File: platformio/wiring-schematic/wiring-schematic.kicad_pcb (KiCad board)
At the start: 2 copper layers, 5 parts, among them U0 LSM9DS1, U1 LSM9DS1, U2 LSM9DS1, U3 LSM9DS1

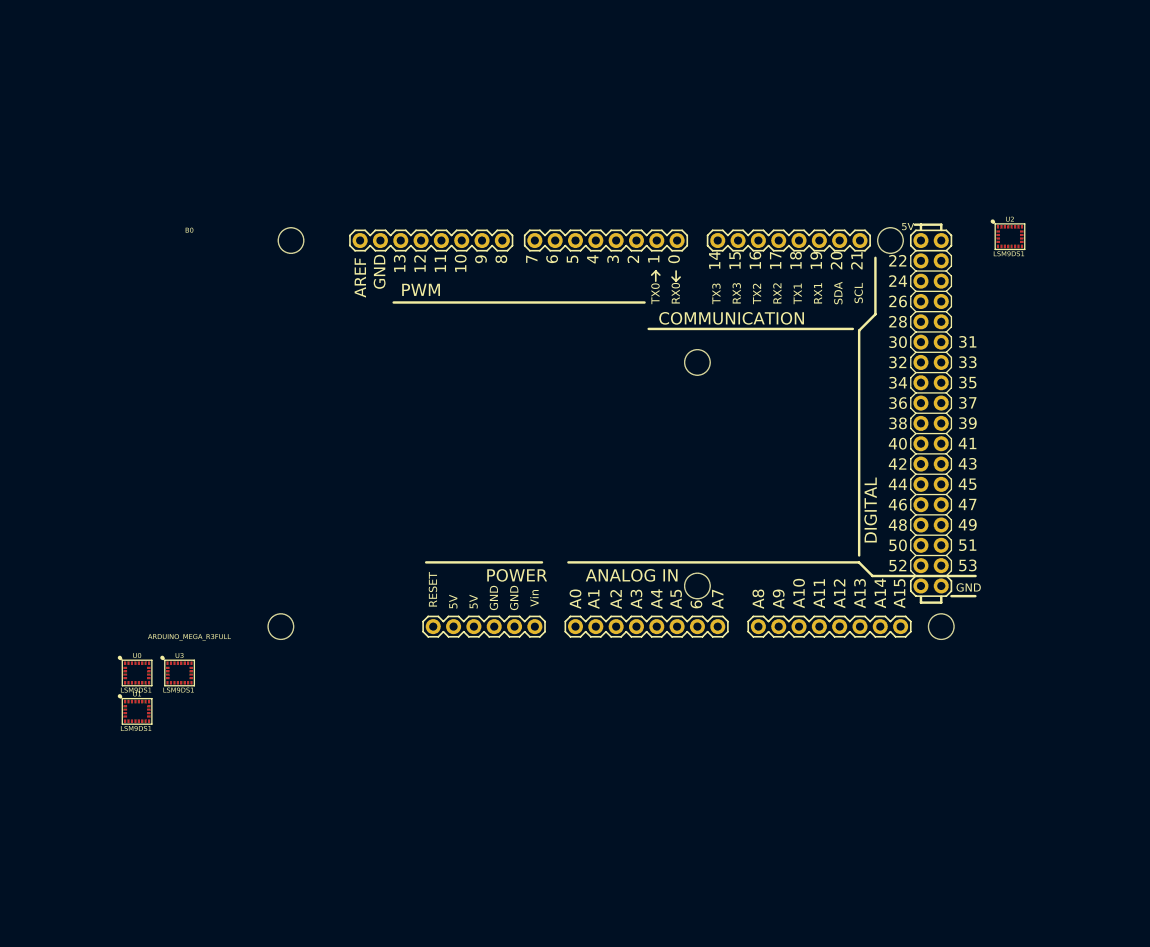
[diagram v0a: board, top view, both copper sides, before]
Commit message: reorganised kicad schematic
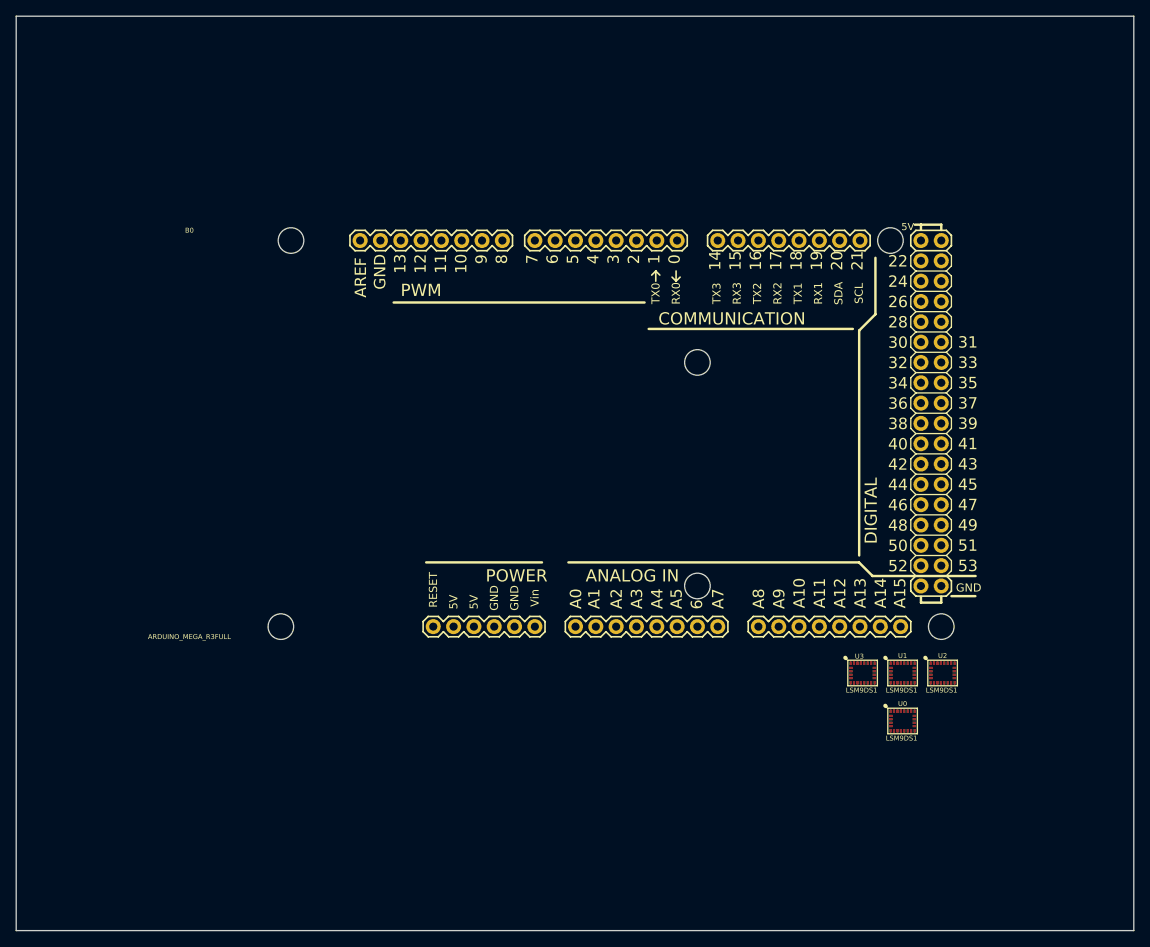
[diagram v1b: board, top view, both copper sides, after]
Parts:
- moved U0 95.9 mm to (695.0, -331.0)
- moved U1 95.8 mm to (695.0, -337.0)
- moved U3 85.4 mm to (690.0, -337.0)
- moved U2 55.2 mm to (700.0, -337.0)
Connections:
- net /CS_MAG_IMU0 renamed /CS_M_0
- net /CS_MAG_IMU1 renamed /CS_M_1
- net /CS_MAG_IMU2 renamed /CS_M_2
- net /CS_MAG_IMU3 renamed /CS_M_3
- B0 pad 0: /CS Accel IMU 0 -> (no net)
- B0 pad 1: /CS Accel IMU 1 -> (no net)
- B0 pad 10: unconnected-(B0-Pad10) -> (no net)
- B0 pad 11: unconnected-(B0-Pad11) -> (no net)
- B0 pad 12: unconnected-(B0-Pad12) -> (no net)
- B0 pad 13: unconnected-(B0-Pad13) -> (no net)
- B0 pad 14: unconnected-(B0-Pad14) -> (no net)
- B0 pad 15: unconnected-(B0-Pad15) -> (no net)
- B0 pad 16: unconnected-(B0-Pad16) -> (no net)
- B0 pad 17: unconnected-(B0-Pad17) -> (no net)
- B0 pad 18: unconnected-(B0-Pad18) -> (no net)
- B0 pad 19: unconnected-(B0-Pad19) -> (no net)
- B0 pad 2: /CS Accel IMU 2 -> (no net)
- B0 pad 24: unconnected-(B0-Pad24) -> (no net)
- B0 pad 25: unconnected-(B0-Pad25) -> (no net)
- B0 pad 26: unconnected-(B0-Pad26) -> (no net)
- B0 pad 27: unconnected-(B0-Pad27) -> (no net)
- B0 pad 28: unconnected-(B0-Pad28) -> (no net)
- B0 pad 29: unconnected-(B0-Pad29) -> (no net)
- B0 pad 3: /CS Accel IMU 3 -> (no net)
- B0 pad 3.3V: unconnected-(B0-Pad3.3V) -> (no net)
- B0 pad 30: unconnected-(B0-Pad30) -> (no net)
- B0 pad 31: unconnected-(B0-Pad31) -> (no net)
- B0 pad 32: unconnected-(B0-Pad32) -> (no net)
- B0 pad 33: unconnected-(B0-Pad33) -> (no net)
- B0 pad 34: unconnected-(B0-Pad34) -> (no net)
- B0 pad 35: unconnected-(B0-Pad35) -> (no net)
- B0 pad 36: unconnected-(B0-Pad36) -> (no net)
- B0 pad 37: unconnected-(B0-Pad37) -> (no net)
- B0 pad 38: unconnected-(B0-Pad38) -> (no net)
- B0 pad 39: unconnected-(B0-Pad39) -> (no net)
- B0 pad 4: unconnected-(B0-Pad4) -> (no net)
- B0 pad 40: unconnected-(B0-Pad40) -> (no net)
- B0 pad 41: unconnected-(B0-Pad41) -> (no net)
- B0 pad 42: unconnected-(B0-Pad42) -> (no net)
- B0 pad 43: unconnected-(B0-Pad43) -> (no net)
- B0 pad 44: unconnected-(B0-Pad44) -> (no net)
- B0 pad 45: unconnected-(B0-Pad45) -> (no net)
- B0 pad 46: unconnected-(B0-Pad46) -> (no net)
- B0 pad 47: unconnected-(B0-Pad47) -> (no net)
- B0 pad 48: unconnected-(B0-Pad48) -> (no net)
- B0 pad 49: unconnected-(B0-Pad49) -> (no net)
- B0 pad 5: unconnected-(B0-Pad5) -> (no net)
- B0 pad 50: /SPI MISO -> (no net)
- B0 pad 53: unconnected-(B0-Pad53) -> (no net)
- B0 pad 5V@0: unconnected-(B0-Pad5V@0) -> (no net)
- B0 pad 5V@1: unconnected-(B0-Pad5V@1) -> (no net)
- B0 pad 5V@2: unconnected-(B0-Pad5V@2) -> (no net)
- B0 pad 6: unconnected-(B0-Pad6) -> (no net)
- B0 pad 7: unconnected-(B0-Pad7) -> (no net)
- B0 pad 8: unconnected-(B0-Pad8) -> (no net)
- B0 pad 9: unconnected-(B0-Pad9) -> (no net)
- B0 pad A0: unconnected-(B0-PadA0) -> (no net)
- B0 pad A1: unconnected-(B0-PadA1) -> (no net)
- B0 pad A10: unconnected-(B0-PadA10) -> (no net)
- B0 pad A11: unconnected-(B0-PadA11) -> (no net)
- B0 pad A12: unconnected-(B0-PadA12) -> (no net)
- B0 pad A13: unconnected-(B0-PadA13) -> (no net)
- B0 pad A14: unconnected-(B0-PadA14) -> (no net)
- B0 pad A15: unconnected-(B0-PadA15) -> (no net)
- B0 pad A2: unconnected-(B0-PadA2) -> (no net)
- B0 pad A3: unconnected-(B0-PadA3) -> (no net)
- B0 pad A4: unconnected-(B0-PadA4) -> (no net)
- B0 pad A5: unconnected-(B0-PadA5) -> (no net)
- B0 pad A6: unconnected-(B0-PadA6) -> (no net)
- B0 pad A7: unconnected-(B0-PadA7) -> (no net)
- B0 pad A8: unconnected-(B0-PadA8) -> (no net)
- B0 pad A9: unconnected-(B0-PadA9) -> (no net)
- B0 pad AREF: unconnected-(B0-PadAREF) -> (no net)
- B0 pad RESE: unconnected-(B0-PadRESE) -> (no net)
- U0 pad 10: unconnected-(U0-Pad10) -> (no net)
- U0 pad 11: unconnected-(U0-Pad11) -> (no net)
- U0 pad 12: unconnected-(U0-Pad12) -> (no net)
- U0 pad 13: unconnected-(U0-Pad13) -> (no net)
- U0 pad 21: unconnected-(U0-Pad21) -> (no net)
- U0 pad 24: unconnected-(U0-Pad24) -> (no net)
- U0 pad 5: unconnected-(U0-Pad5) -> (no net)
- U0 pad 6: unconnected-(U0-Pad6) -> (no net)
- U0 pad 7: /CS Accel IMU 0 -> (no net)
- U0 pad 9: unconnected-(U0-Pad9) -> (no net)
- U1 pad 10: unconnected-(U1-Pad10) -> (no net)
- U1 pad 11: unconnected-(U1-Pad11) -> (no net)
- U1 pad 12: unconnected-(U1-Pad12) -> (no net)
- U1 pad 13: unconnected-(U1-Pad13) -> (no net)
- U1 pad 21: unconnected-(U1-Pad21) -> (no net)
- U1 pad 24: unconnected-(U1-Pad24) -> (no net)
- U1 pad 5: unconnected-(U1-Pad5) -> (no net)
- U1 pad 6: unconnected-(U1-Pad6) -> (no net)
- U1 pad 7: /CS Accel IMU 1 -> (no net)
- U1 pad 9: unconnected-(U1-Pad9) -> (no net)
- U2 pad 10: unconnected-(U2-Pad10) -> (no net)
- U2 pad 11: unconnected-(U2-Pad11) -> (no net)
- U2 pad 12: unconnected-(U2-Pad12) -> (no net)
- U2 pad 13: unconnected-(U2-Pad13) -> (no net)
- U2 pad 21: unconnected-(U2-Pad21) -> (no net)
- U2 pad 24: unconnected-(U2-Pad24) -> (no net)
- U2 pad 5: unconnected-(U2-Pad5) -> (no net)
- U2 pad 6: unconnected-(U2-Pad6) -> (no net)
- U2 pad 7: /CS Accel IMU 2 -> (no net)
- U2 pad 9: unconnected-(U2-Pad9) -> (no net)
- U3 pad 10: unconnected-(U3-Pad10) -> (no net)
- U3 pad 11: unconnected-(U3-Pad11) -> (no net)
- U3 pad 12: unconnected-(U3-Pad12) -> (no net)
- U3 pad 13: unconnected-(U3-Pad13) -> (no net)
- U3 pad 21: unconnected-(U3-Pad21) -> (no net)
- U3 pad 24: unconnected-(U3-Pad24) -> (no net)
- U3 pad 5: unconnected-(U3-Pad5) -> (no net)
- U3 pad 6: unconnected-(U3-Pad6) -> (no net)
- U3 pad 7: /CS Accel IMU 3 -> (no net)
- U3 pad 9: unconnected-(U3-Pad9) -> (no net)
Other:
- board outline added: 139.7 x 114.3 mm

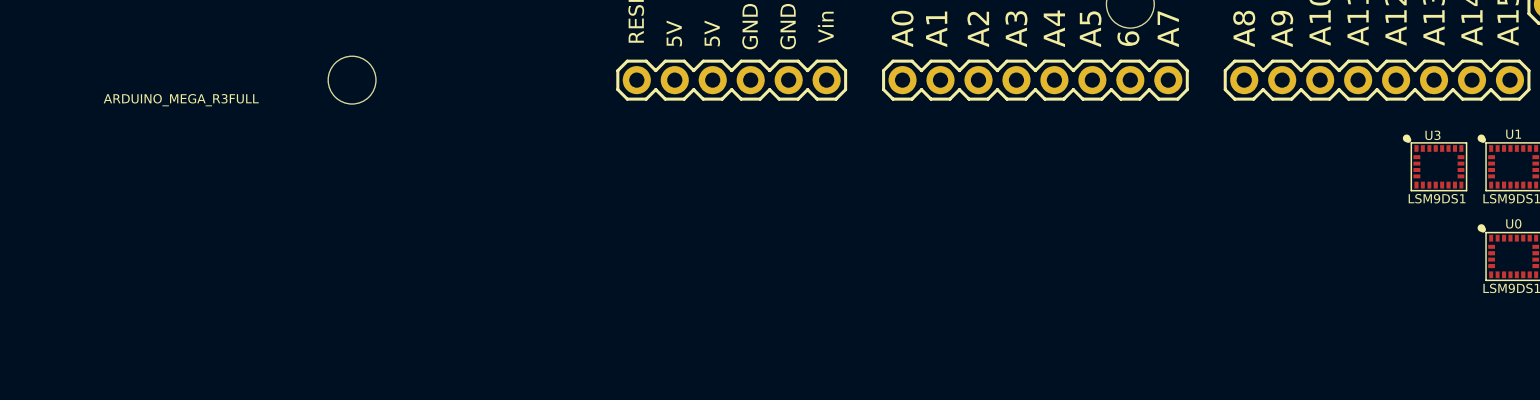
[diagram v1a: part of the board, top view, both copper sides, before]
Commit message: Finalised kicad schematic, and exported SVG
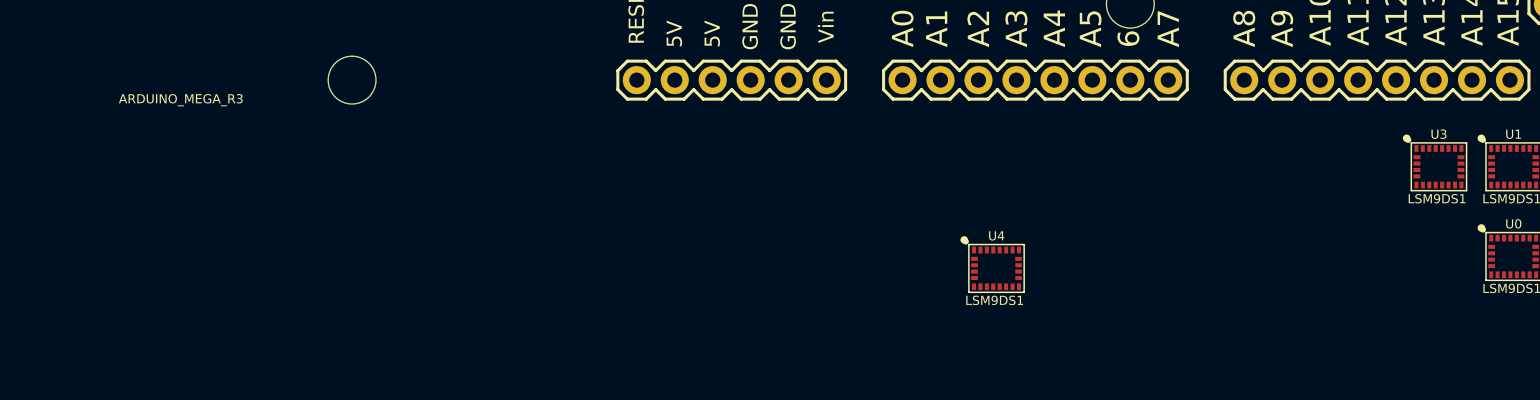
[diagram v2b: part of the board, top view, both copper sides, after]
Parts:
- added U4: LSM9DS1, SparkFun-Silicon-Custom:LGA-24-3.5X3, F.Cu at (660.4, -330.2)
- B0: value ARDUINO_MEGA_R3FULL -> ARDUINO_MEGA_R3
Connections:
- net +5V renamed 5V
- B0 pad 0: (no net) -> unconnected-(B0-Pad0)
- B0 pad 1: (no net) -> unconnected-(B0-Pad1)
- B0 pad 10: (no net) -> unconnected-(B0-Pad10)
- B0 pad 11: (no net) -> unconnected-(B0-Pad11)
- B0 pad 12: (no net) -> unconnected-(B0-Pad12)
- B0 pad 13: (no net) -> unconnected-(B0-Pad13)
- B0 pad 14: (no net) -> unconnected-(B0-Pad14)
- B0 pad 15: (no net) -> unconnected-(B0-Pad15)
- B0 pad 16: (no net) -> unconnected-(B0-Pad16)
- B0 pad 17: (no net) -> unconnected-(B0-Pad17)
- B0 pad 18: (no net) -> unconnected-(B0-Pad18)
- B0 pad 19: (no net) -> unconnected-(B0-Pad19)
- B0 pad 2: (no net) -> unconnected-(B0-Pad2)
- B0 pad 20: /CS_M_0 -> unconnected-(B0-Pad20)
- B0 pad 21: /CS_M_1 -> unconnected-(B0-Pad21)
- B0 pad 22: /CS_M_2 -> unconnected-(B0-Pad22)
- B0 pad 23: /CS_M_3 -> unconnected-(B0-Pad23)
- B0 pad 24: (no net) -> unconnected-(B0-Pad24)
- B0 pad 25: (no net) -> unconnected-(B0-Pad25)
- B0 pad 26: (no net) -> unconnected-(B0-Pad26)
- B0 pad 27: (no net) -> /CS_MAG_0
- B0 pad 28: (no net) -> /CS_ACC_0
- B0 pad 29: (no net) -> /CS_MAG_1
- B0 pad 3: (no net) -> unconnected-(B0-Pad3)
- B0 pad 3.3V: (no net) -> unconnected-(B0-Pad3.3V)
- B0 pad 30: (no net) -> /CS_ACC_1
- B0 pad 31: (no net) -> /CS_MAG_2
- B0 pad 32: (no net) -> /CS_ACC_2
- B0 pad 33: (no net) -> /CS_MAG_3
- B0 pad 34: (no net) -> /CS_ACC_3
- B0 pad 35: (no net) -> /CS_MAG_4
- B0 pad 36: (no net) -> /CS_ACC_4
- B0 pad 37: (no net) -> unconnected-(B0-Pad37)
- B0 pad 38: (no net) -> unconnected-(B0-Pad38)
- B0 pad 39: (no net) -> unconnected-(B0-Pad39)
- B0 pad 4: (no net) -> unconnected-(B0-Pad4)
- B0 pad 40: (no net) -> unconnected-(B0-Pad40)
- B0 pad 41: (no net) -> unconnected-(B0-Pad41)
- B0 pad 42: (no net) -> unconnected-(B0-Pad42)
- B0 pad 43: (no net) -> unconnected-(B0-Pad43)
- B0 pad 44: (no net) -> unconnected-(B0-Pad44)
- B0 pad 45: (no net) -> unconnected-(B0-Pad45)
- B0 pad 46: (no net) -> unconnected-(B0-Pad46)
- B0 pad 47: (no net) -> unconnected-(B0-Pad47)
- B0 pad 48: (no net) -> unconnected-(B0-Pad48)
- B0 pad 49: (no net) -> unconnected-(B0-Pad49)
- B0 pad 5: (no net) -> unconnected-(B0-Pad5)
- B0 pad 50: (no net) -> unconnected-(B0-Pad50)
- B0 pad 53: (no net) -> unconnected-(B0-Pad53)
- B0 pad 5V@0: (no net) -> unconnected-(B0-Pad5V@0)
- B0 pad 5V@1: (no net) -> unconnected-(B0-Pad5V@1)
- B0 pad 5V@2: (no net) -> unconnected-(B0-Pad5V@2)
- B0 pad 6: (no net) -> unconnected-(B0-Pad6)
- B0 pad 7: (no net) -> unconnected-(B0-Pad7)
- B0 pad 8: (no net) -> unconnected-(B0-Pad8)
- B0 pad 9: (no net) -> unconnected-(B0-Pad9)
- B0 pad A0: (no net) -> unconnected-(B0-PadA0)
- B0 pad A1: (no net) -> unconnected-(B0-PadA1)
- B0 pad A10: (no net) -> unconnected-(B0-PadA10)
- B0 pad A11: (no net) -> unconnected-(B0-PadA11)
- B0 pad A12: (no net) -> unconnected-(B0-PadA12)
- B0 pad A13: (no net) -> unconnected-(B0-PadA13)
- B0 pad A14: (no net) -> unconnected-(B0-PadA14)
- B0 pad A15: (no net) -> unconnected-(B0-PadA15)
- B0 pad A2: (no net) -> unconnected-(B0-PadA2)
- B0 pad A3: (no net) -> unconnected-(B0-PadA3)
- B0 pad A4: (no net) -> unconnected-(B0-PadA4)
- B0 pad A5: (no net) -> unconnected-(B0-PadA5)
- B0 pad A6: (no net) -> unconnected-(B0-PadA6)
- B0 pad A7: (no net) -> unconnected-(B0-PadA7)
- B0 pad A8: (no net) -> unconnected-(B0-PadA8)
- B0 pad A9: (no net) -> unconnected-(B0-PadA9)
- B0 pad AREF: (no net) -> unconnected-(B0-PadAREF)
- B0 pad RESE: (no net) -> unconnected-(B0-PadRESE)
- U0 pad 10: (no net) -> unconnected-(U0-Pad10)
- U0 pad 11: (no net) -> unconnected-(U0-Pad11)
- U0 pad 12: (no net) -> unconnected-(U0-Pad12)
- U0 pad 13: (no net) -> unconnected-(U0-Pad13)
- U0 pad 21: (no net) -> unconnected-(U0-Pad21)
- U0 pad 24: (no net) -> unconnected-(U0-Pad24)
- U0 pad 5: (no net) -> unconnected-(U0-Pad5)
- U0 pad 6: (no net) -> unconnected-(U0-Pad6)
- U0 pad 7: (no net) -> /CS_ACC_0
- U0 pad 8: /CS_M_0 -> /CS_MAG_0
- U0 pad 9: (no net) -> unconnected-(U0-Pad9)
- U1 pad 10: (no net) -> unconnected-(U1-Pad10)
- U1 pad 11: (no net) -> unconnected-(U1-Pad11)
- U1 pad 12: (no net) -> unconnected-(U1-Pad12)
- U1 pad 13: (no net) -> unconnected-(U1-Pad13)
- U1 pad 21: (no net) -> unconnected-(U1-Pad21)
- U1 pad 24: (no net) -> unconnected-(U1-Pad24)
- U1 pad 5: (no net) -> unconnected-(U1-Pad5)
- U1 pad 6: (no net) -> unconnected-(U1-Pad6)
- U1 pad 7: (no net) -> /CS_ACC_1
- U1 pad 8: /CS_M_1 -> /CS_MAG_1
- U1 pad 9: (no net) -> unconnected-(U1-Pad9)
- U2 pad 10: (no net) -> unconnected-(U2-Pad10)
- U2 pad 11: (no net) -> unconnected-(U2-Pad11)
- U2 pad 12: (no net) -> unconnected-(U2-Pad12)
- U2 pad 13: (no net) -> unconnected-(U2-Pad13)
- U2 pad 21: (no net) -> unconnected-(U2-Pad21)
- U2 pad 24: (no net) -> unconnected-(U2-Pad24)
- U2 pad 5: (no net) -> unconnected-(U2-Pad5)
- U2 pad 6: (no net) -> unconnected-(U2-Pad6)
- U2 pad 7: (no net) -> /CS_ACC_2
- U2 pad 8: /CS_M_2 -> /CS_MAG_2
- U2 pad 9: (no net) -> unconnected-(U2-Pad9)
- U3 pad 10: (no net) -> unconnected-(U3-Pad10)
- U3 pad 11: (no net) -> unconnected-(U3-Pad11)
- U3 pad 12: (no net) -> unconnected-(U3-Pad12)
- U3 pad 13: (no net) -> unconnected-(U3-Pad13)
- U3 pad 21: (no net) -> unconnected-(U3-Pad21)
- U3 pad 24: (no net) -> unconnected-(U3-Pad24)
- U3 pad 5: (no net) -> unconnected-(U3-Pad5)
- U3 pad 6: (no net) -> unconnected-(U3-Pad6)
- U3 pad 7: (no net) -> /CS_ACC_3
- U3 pad 8: /CS_M_3 -> /CS_MAG_3
- U3 pad 9: (no net) -> unconnected-(U3-Pad9)
